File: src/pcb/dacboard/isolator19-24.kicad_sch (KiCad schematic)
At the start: 18 parts, among them U101 ISO7761FQDBQRQ1, U102 ISO7761FQDBQRQ1, U103 ISO7761FQDBQRQ1, U104 ISO7761FQDBQRQ1, U105 ISO7761FQDBQRQ1, U106 ISO7761FQDBQRQ1

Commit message: dacboard routing
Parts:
- removed U101, U102, U103, U104, U105, U106: ISO7761FQDBQRQ1, DBQ16_TEX, symbol 2025-11-18_20-36-36:ISO7761FQDBQRQ1
- added U100, U101, U102, U103, U104, U105: ISO6761FQDWRQ1, ISO6761:SOIC16_DW_TEX, symbol 2025-11-20_00-47-15:ISO6761FQDWRQ1
- C108, C109, C110, C111, C112, C113, C114, C115, C116, C117, C118, C119: footprint (none) -> Capacitor_SMD:C_0402_1005Metric_Pad0.74x0.62mm_HandSolder
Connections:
- net +5VD: now also U100.16 (VCC2), U101.16 (VCC2), U102.16 (VCC2), U103.16 (VCC2), U104.16 (VCC2), U105.16 (VCC2)
- net CS_N_CH19: now also U100.5 (IND)
- net CS_N_CH20: now also U101.5 (IND)
- net CS_N_CH21: now also U102.5 (IND)
- net CS_N_CH22: now also U103.5 (IND)
- net CS_N_CH23: now also U104.5 (IND)
- net CS_N_CH24: now also U105.5 (IND)
- net DAC19_LDAC_N: now also U100.15 (OUTA)
- net DAC19_SCLK: now also U100.13 (OUTC)
- net DAC19_SDIN: now also U100.14 (OUTB)
- net DAC19_SDO: now also U100.10 (INF)
- net DAC19_SYNC_N: now also U100.12 (OUTD)
- net DAC20_LDAC_N: now also U101.15 (OUTA)
- net DAC20_SCLK: now also U101.13 (OUTC)
- net DAC20_SDIN: now also U101.14 (OUTB)
- net DAC20_SDO: now also U101.10 (INF)
- net DAC20_SYNC_N: now also U101.12 (OUTD)
- net DAC21_LDAC_N: now also U102.15 (OUTA)
- net DAC21_SCLK: now also U102.13 (OUTC)
- net DAC21_SDIN: now also U102.14 (OUTB)
- net DAC21_SDO: now also U102.10 (INF)
- net DAC21_SYNC_N: now also U102.12 (OUTD)
- net DAC22_LDAC_N: now also U103.15 (OUTA)
- net DAC22_SCLK: now also U103.13 (OUTC)
- net DAC22_SDIN: now also U103.14 (OUTB)
- net DAC22_SDO: now also U103.10 (INF)
- net DAC22_SYNC_N: now also U103.12 (OUTD)
- net DAC23_LDAC_N: now also U104.15 (OUTA)
- net DAC23_SCLK: now also U104.13 (OUTC)
- net DAC23_SDIN: now also U104.14 (OUTB)
- net DAC23_SDO: now also U104.10 (INF)
- net DAC23_SYNC_N: now also U104.12 (OUTD)
- net DAC24_LDAC_N: now also U105.15 (OUTA)
- net DAC24_SCLK: now also U105.13 (OUTC)
- net DAC24_SDIN: now also U105.14 (OUTB)
- net DAC24_SDO: now also U105.10 (INF)
- net DAC24_SYNC_N: now also U105.12 (OUTD)
- net DGND: now also U100.9 (GND2), U101.9 (GND2), U102.9 (GND2), U103.9 (GND2), U104.9 (GND2), U105.9 (GND2)
- net LDAC_N_CH19: now also U100.2 (INA)
- net LDAC_N_CH20: now also U101.2 (INA)
- net LDAC_N_CH21: now also U102.2 (INA)
- net LDAC_N_CH22: now also U103.2 (INA)
- net LDAC_N_CH23: now also U104.2 (INA)
- net LDAC_N_CH24: now also U105.2 (INA)
- net MISO_CH19: now also U100.7 (OUTF)
- net MISO_CH20: now also U101.7 (OUTF)
- net MISO_CH21: now also U102.7 (OUTF)
- net MISO_CH22: now also U103.7 (OUTF)
- net MISO_CH23: now also U104.7 (OUTF)
- net MISO_CH24: now also U105.7 (OUTF)
- net MOSI_CH19: now also U100.3 (INB)
- net MOSI_CH20: now also U101.3 (INB)
- net MOSI_CH21: now also U102.3 (INB)
- net MOSI_CH22: now also U103.3 (INB)
- net MOSI_CH23: now also U104.3 (INB)
- net MOSI_CH24: now also U105.3 (INB)
- net NGND: now also U100.8 (GND1), U101.8 (GND1), U102.8 (GND1), U103.8 (GND1), U104.8 (GND1), U105.8 (GND1)
- net SCLK_CH19: now also U100.4 (INC)
- net SCLK_CH20: now also U101.4 (INC)
- net SCLK_CH21: now also U102.4 (INC)
- net SCLK_CH22: now also U103.4 (INC)
- net SCLK_CH23: now also U104.4 (INC)
- net SCLK_CH24: now also U105.4 (INC)
- net +3V3N renamed VCCN
- net VCCN: now also U100.1 (VCC1), U101.1 (VCC1), U102.1 (VCC1), U103.1 (VCC1), U104.1 (VCC1), U105.1 (VCC1)

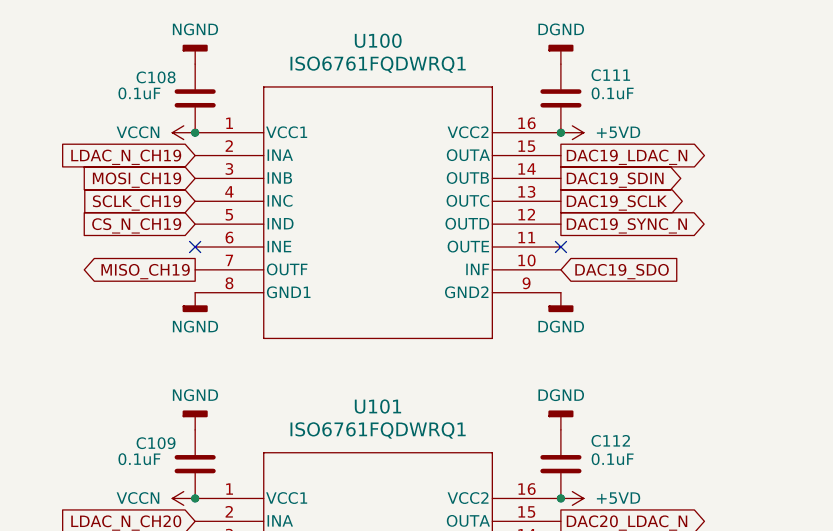
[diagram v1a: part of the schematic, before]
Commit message: low noise digital finished
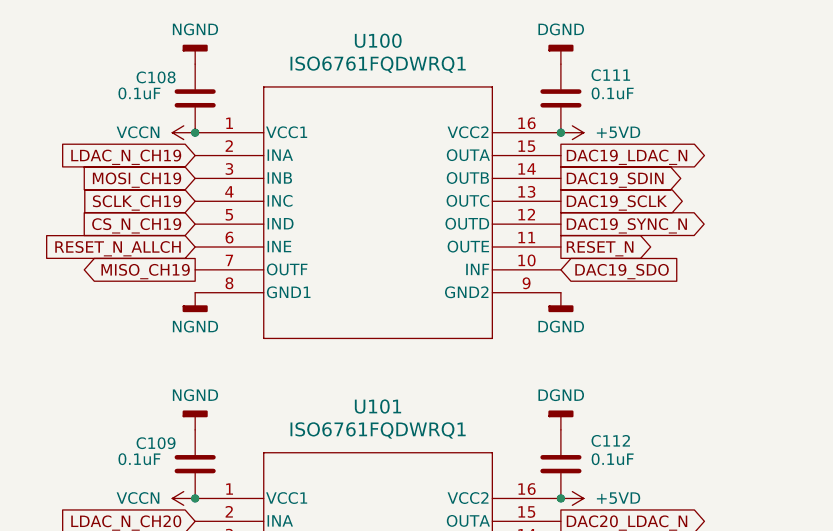
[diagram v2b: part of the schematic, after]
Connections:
- net RESET_N: now reaches U100.11 (OUTE)
- net RESET_N_ALLCH: now reaches U100.6 (INE)
- no-connect marks 12 -> 10
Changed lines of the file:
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@@
-	)
-	(no_connect
-		(at 115.57 57.15)
 	)
 	(no_connect
@@
 	)
 	(no_connect
-		(at 74.93 57.15)
-	)
-	(no_connect
 		(at 74.93 97.79)
 	)
@@
 			(effects
 				(font
+					(size 1.27 1.27)
+				)
+				(justify right)
+				(hide yes)
+			)
+		)
+	)
+	(global_label "RESET_N"
+		(shape output)
+		(at 115.57 57.15 0)
+		(fields_autoplaced yes)
+		(effects
+			(font
+				(size 1.27 1.27)
+			)
+			(justify left)
+		)
+		(property "Intersheetrefs" "${INTERSHEET_REFS}"
+			(at 126.5984 57.15 0)
+			(effects
+				(font
+					(size 1.27 1.27)
+				)
+				(justify left)
+				(hide yes)
+			)
+		)
+	)
+	(global_label "RESET_N_ALLCH"
+		(shape input)
+		(at 74.93 57.15 180)
+		(fields_autoplaced yes)
+		(effects
+			(font
+				(size 1.27 1.27)
+			)
+			(justify right)
+		)
+		(property "Intersheetrefs" "${INTERSHEET_REFS}"
+			(at 57.1887 57.15 0)
+			(effects
+				(font

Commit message: adding more capacitors to analog side
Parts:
- U100, U101, U102, U103, U104, U105: footprint ISO6761:SOIC16_DW_TEX -> Package_SO:SOIC-16W_7.5x10.3mm_P1.27mm
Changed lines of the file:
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@@
 			)
 		)
-		(property "Footprint" "ISO6761:SOIC16_DW_TEX"
+		(property "Footprint" "Package_SO:SOIC-16W_7.5x10.3mm_P1.27mm"
 			(at 74.93 44.45 0)
 			(effects
@@
 			)
 		)
-		(property "Footprint" "ISO6761:SOIC16_DW_TEX"
+		(property "Footprint" "Package_SO:SOIC-16W_7.5x10.3mm_P1.27mm"
 			(at 173.99 44.45 0)
 			(effects
@@
 			)
 		)
-		(property "Footprint" "ISO6761:SOIC16_DW_TEX"
+		(property "Footprint" "Package_SO:SOIC-16W_7.5x10.3mm_P1.27mm"
 			(at 173.99 127 0)
 			(effects
@@
 			)
 		)
-		(property "Footprint" "ISO6761:SOIC16_DW_TEX"
+		(property "Footprint" "Package_SO:SOIC-16W_7.5x10.3mm_P1.27mm"
 			(at 74.93 85.09 0)
 			(effects
@@
 			)
 		)
-		(property "Footprint" "ISO6761:SOIC16_DW_TEX"
+		(property "Footprint" "Package_SO:SOIC-16W_7.5x10.3mm_P1.27mm"
 			(at 173.99 85.09 0)
 			(effects
@@
 			)
 		)
-		(property "Footprint" "ISO6761:SOIC16_DW_TEX"
+		(property "Footprint" "Package_SO:SOIC-16W_7.5x10.3mm_P1.27mm"
 			(at 74.93 127 0)
 			(effects
